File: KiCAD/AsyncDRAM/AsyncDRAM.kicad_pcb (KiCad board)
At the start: 2 copper layers, 54.6 x 33.7 mm, 14 parts, among them J1 UART, J2 SPI, J3 UPDI, J4 POWER

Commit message: Finished Routing PCB
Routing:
- net ~W: track 31.8 -> 71.0 mm, vias 2 -> 4
- net ~RAS: track 19.3 -> 47.8 mm, vias 2 -> 3
- net UPDI: track 0.00 -> 23.2 mm, vias 0 -> 1
- net ~CAS: track 28.4 -> 47.1 mm
- net +5V: track 124.1 -> 141.6 mm
- net ~OE: track 27.8 -> 43.7 mm
- net D3: track 36.5 -> 35.1 mm

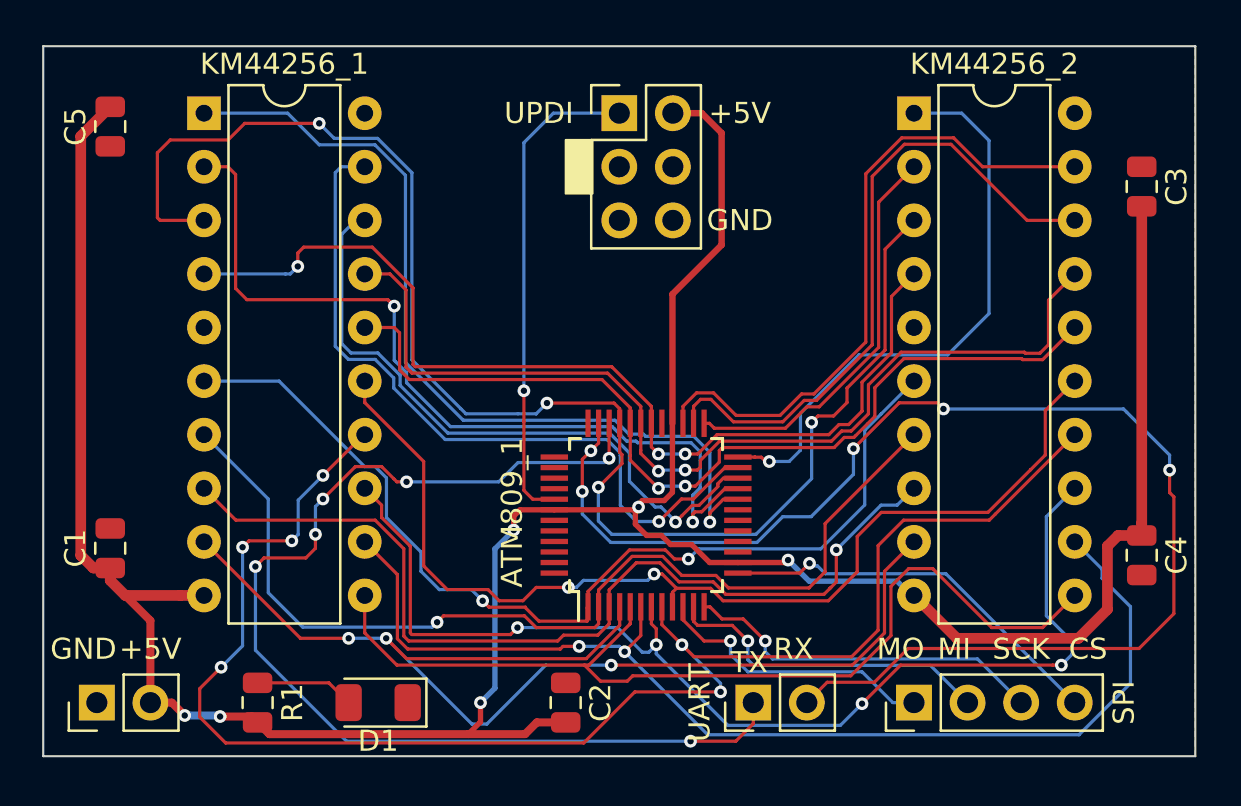
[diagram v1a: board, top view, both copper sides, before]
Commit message: Beautify the Traces + Gerber Output
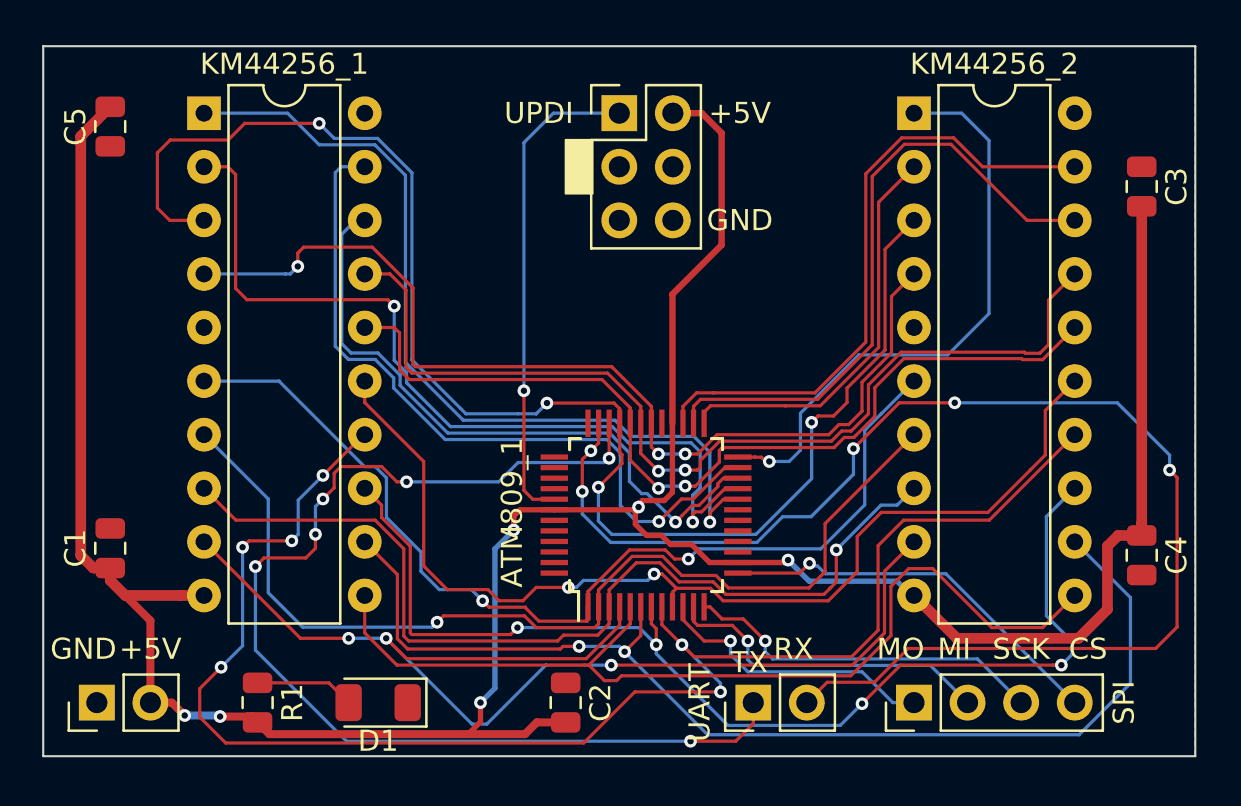
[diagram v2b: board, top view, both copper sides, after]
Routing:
- net D7: track 30.8 -> 29.9 mm
- net D6: track 31.1 -> 30.2 mm
- net RxD: track 64.4 -> 65.0 mm

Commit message: Finalized silkscreen
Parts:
- renumbered ATM809_1 to ATmega809, KM44256_1 to KM44C256BP-8, KM44256_2 to KM44C256BP-8
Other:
- board text added: "100nF"
- board text added: "470Ω"
- board text added: "47uF"
- board text added: "JLCJLCJLCJLC"

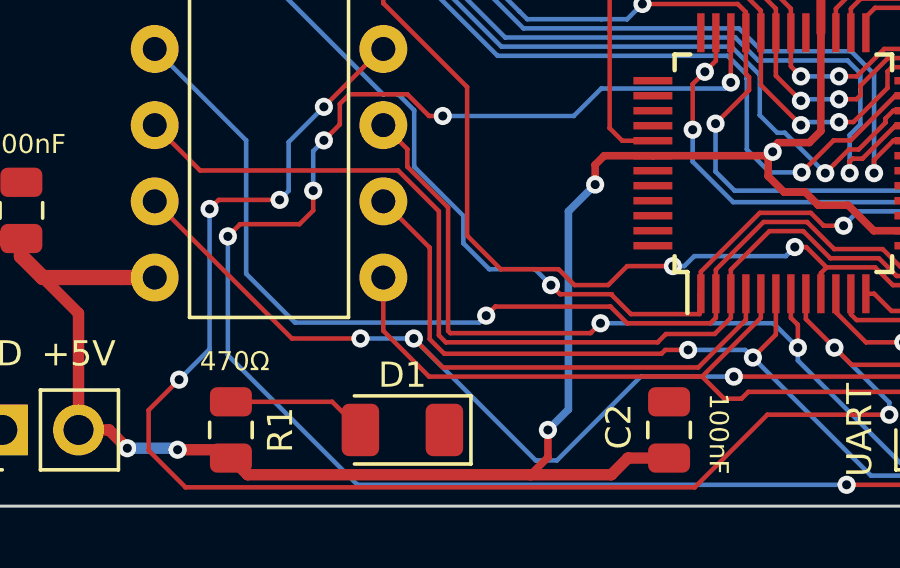
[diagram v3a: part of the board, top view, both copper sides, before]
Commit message: Re-routed power line from decoupling capacitor
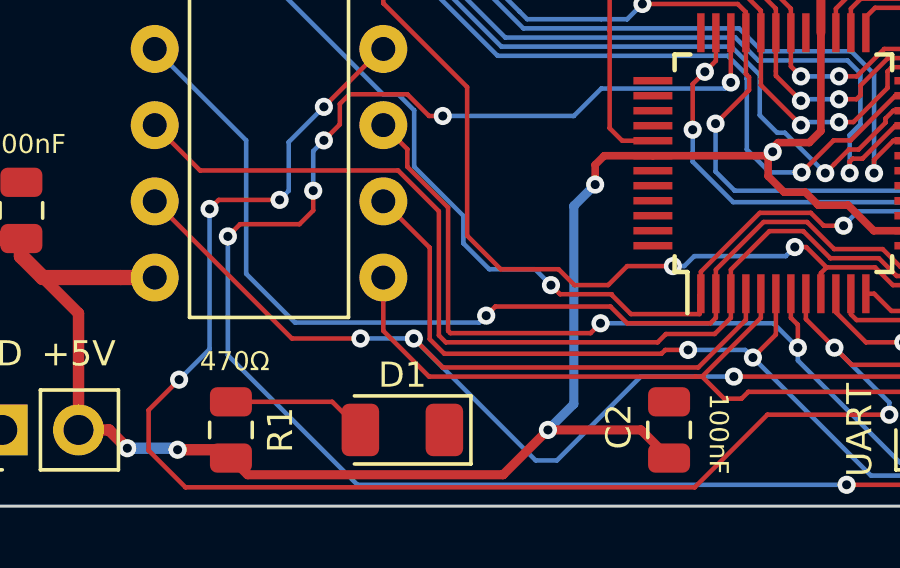
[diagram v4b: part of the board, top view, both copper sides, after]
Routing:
- net +5V: track 141.6 -> 140.6 mm
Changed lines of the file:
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@@
     (thickness 1.6)
     (drawings 23)
-    (tracks 700)
+    (tracks 698)
     (zones 0)
     (modules 14)
@@
   )
   (setup
-    (last_trace_width 0.1524)
+    (last_trace_width 0.3048)
     (user_trace_width 0.1524)
     (user_trace_width 0.2032)
@@
   (segment (start 23.5712 193.6496) (end 23.622 193.7004) (width 0.381) (layer B.Cu) (net 4))
   (segment (start 21.9456 193.6496) (end 23.5712 193.6496) (width 0.381) (layer B.Cu) (net 4))
-  (segment (start 25.4 193.9775) (end 25.956237 194.533737) (width 0.381) (layer F.Cu) (net 4))
-  (segment (start 38.6357 193.9775) (end 40.005 193.9775) (width 0.381) (layer F.Cu) (net 4))
-  (segment (start 38.079463 194.533737) (end 38.6357 193.9775) (width 0.381) (layer F.Cu) (net 4))
-  (segment (start 36.649801 185.752599) (end 36.649801 192.356599) (width 0.254) (layer B.Cu) (net 4))
-  (segment (start 37.5412 184.8612) (end 36.649801 185.752599) (width 0.254) (layer B.Cu) (net 4))
-  (segment (start 36.649801 192.356599) (end 35.9664 193.04) (width 0.254) (layer B.Cu) (net 4))
   (segment (start 35.9664 193.04) (end 35.9664 193.04) (width 0.254) (layer B.Cu) (net 4))
   (via (at 35.9664 193.04) (size 0.6048) (drill 0.3) (layers F.Cu B.Cu) (net 4))
-  (segment (start 35.9664 193.9544) (end 35.387063 194.533737) (width 0.254) (layer F.Cu) (net 4))
-  (segment (start 35.9664 193.04) (end 35.9664 193.9544) (width 0.254) (layer F.Cu) (net 4))
-  (segment (start 25.956237 194.533737) (end 35.387063 194.533737) (width 0.381) (layer F.Cu) (net 4))
-  (segment (start 35.387063 194.533737) (end 38.079463 194.533737) (width 0.381) (layer F.Cu) (net 4))
   (segment (start 58.547 189.992) (end 64.3128 189.992) (width 0.508) (layer F.Cu) (net 4))
   (segment (start 66.1901 185.1175) (end 67.31 185.1175) (width 0.508) (layer F.Cu) (net 4))
@@
   (segment (start 46.4566 165.1) (end 45.085 165.1) (width 0.3048) (layer F.Cu) (net 4))
   (segment (start 47.3964 166.0398) (end 46.4566 165.1) (width 0.3048) (layer F.Cu) (net 4))
+  (segment (start 39.0675 193.04) (end 35.9664 193.04) (width 0.3048) (layer F.Cu) (net 4))
+  (segment (start 40.005 193.9775) (end 39.0675 193.04) (width 0.3048) (layer F.Cu) (net 4))
+  (segment (start 25.956237 194.533737) (end 25.4 193.9775) (width 0.3048) (layer F.Cu) (net 4))
+  (segment (start 34.472663 194.533737) (end 25.956237 194.533737) (width 0.3048) (layer F.Cu) (net 4))
+  (segment (start 35.9664 193.04) (end 34.472663 194.533737) (width 0.3048) (layer F.Cu) (net 4))
+  (segment (start 36.83 185.5724) (end 37.5412 184.8612) (width 0.3048) (layer B.Cu) (net 4))
+  (segment (start 35.9664 193.04) (end 36.83 192.1764) (width 0.3048) (layer B.Cu) (net 4))
+  (segment (start 36.83 192.1764) (end 36.83 185.5724) (width 0.3048) (layer B.Cu) (net 4))
   (via (at 44.4246 184.4548) (size 0.6048) (drill 0.3) (layers F.Cu B.Cu) (net 8))
   (segment (start 47.547452 181.9) (end 46.059452 183.388) (width 0.1524) (layer F.Cu) (net 8))

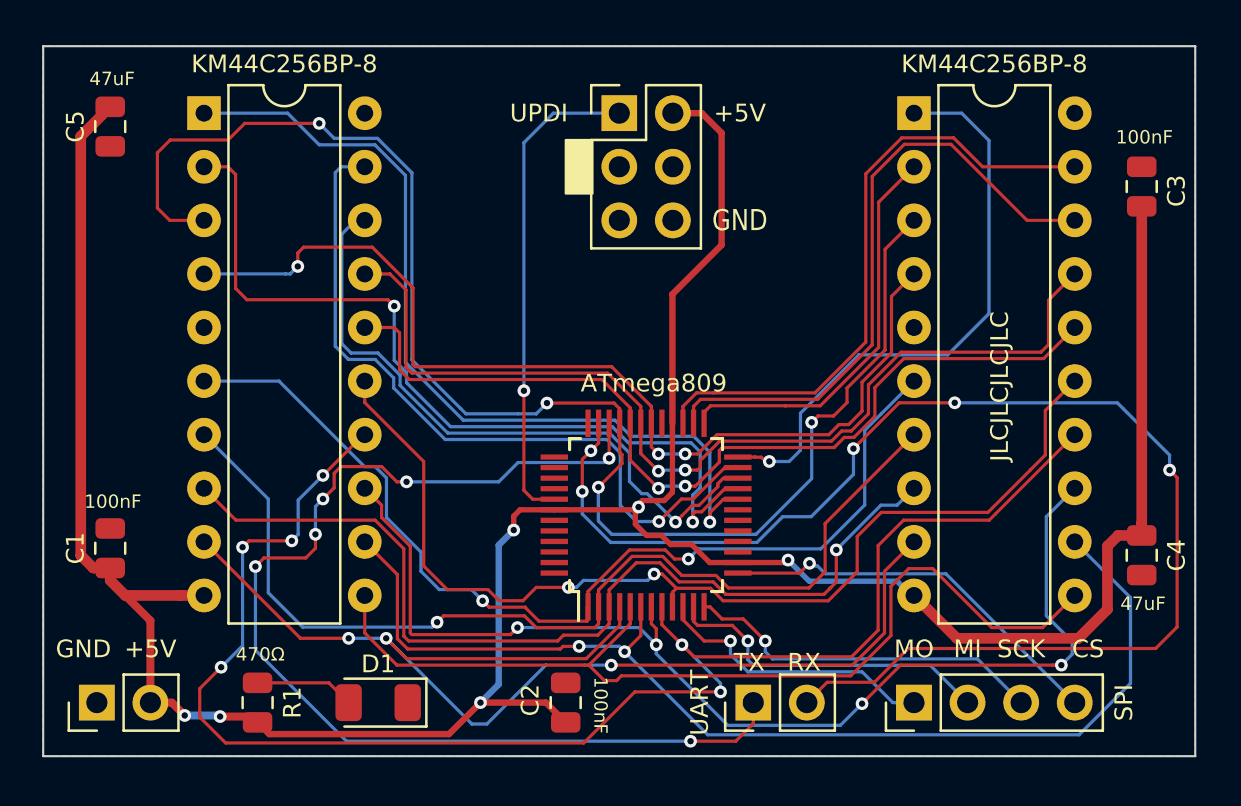
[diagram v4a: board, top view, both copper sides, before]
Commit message: Added more silk screen
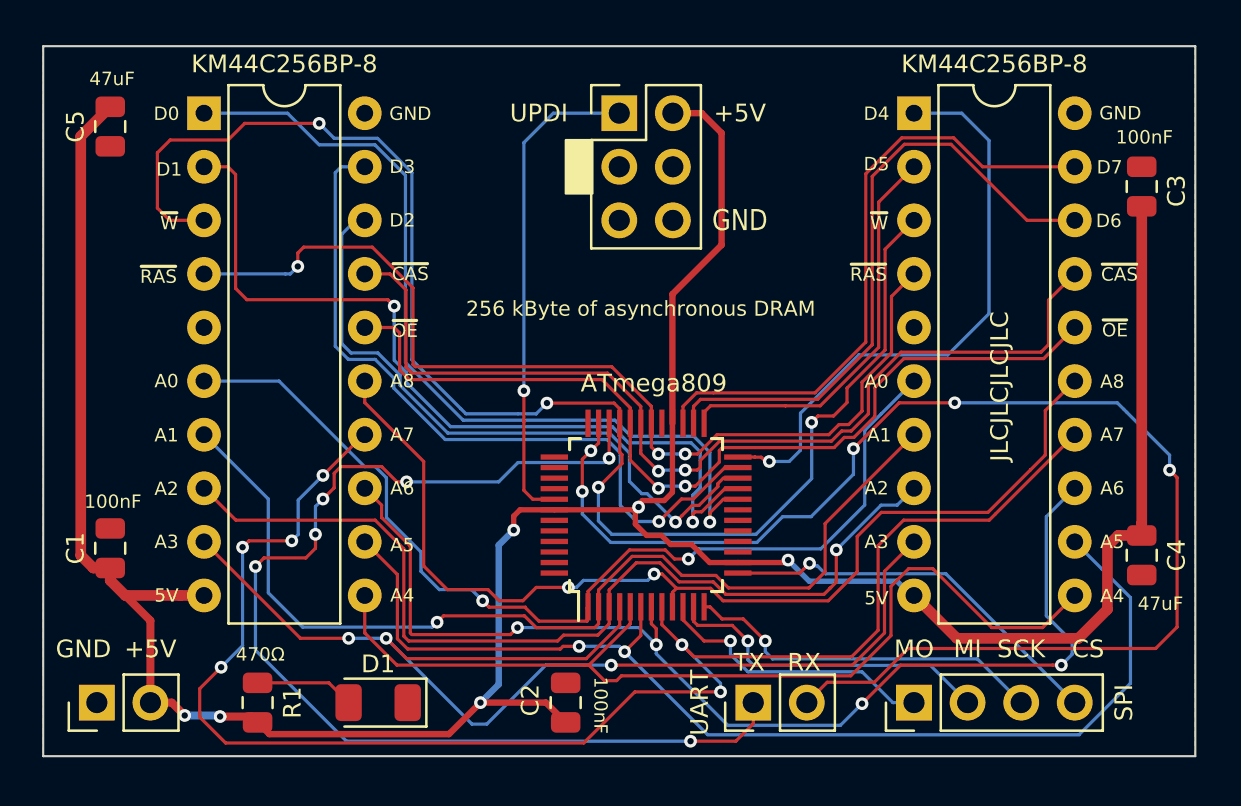
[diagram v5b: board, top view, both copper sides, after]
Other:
- board text added: "256 kByte of asynchronous DRAM"
- board text added: "5V"
- board text added: "A0"
- board text added: "A1"
- board text added: "A2"
- board text added: "A3"
- board text added: "A4"
- board text added: "A5"
- board text added: "A6"
- board text added: "A7"
- board text added: "A8"
- board text added: "D0"
- board text added: "D1"
- board text added: "D2"
- board text added: "D3"
- board text added: "D4"
- board text added: "D5"
- board text added: "D6"
- board text added: "D7"
- board text added: "~CAS"
- board text added: "~OE"
- board text added: "~RAS"
- board text added: "~W"
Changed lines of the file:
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@@
   (general
     (thickness 1.6)
-    (drawings 23)
+    (drawings 62)
     (tracks 698)
     (zones 0)
@@
   )
   (setup
-    (last_trace_width 0.3048)
+    (last_trace_width 0.1524)
     (user_trace_width 0.1524)
     (user_trace_width 0.2032)
@@
     )
   )
+  (gr_text "256 kByte of asynchronous DRAM" (at 43.561 174.371) (layer F.SilkS)
+    (effects (font (size 0.7112 0.7112) (thickness 0.15)))
+  )
+  (gr_text A4 (at 65.913 187.9854) (layer F.SilkS)
+    (effects (font (size 0.635 0.635) (thickness 0.15)))
+  )
+  (gr_text A5 (at 65.913 185.42) (layer F.SilkS)
+    (effects (font (size 0.635 0.635) (thickness 0.15)))
+  )
+  (gr_text A6 (at 65.913 182.88) (layer F.SilkS)
+    (effects (font (size 0.635 0.635) (thickness 0.15)))
+  )
+  (gr_text A7 (at 65.913 180.34) (layer F.SilkS)
+    (effects (font (size 0.635 0.635) (thickness 0.15)))
+  )
+  (gr_text A8 (at 65.913 177.8254) (layer F.SilkS)
+    (effects (font (size 0.635 0.635) (thickness 0.15)))
+  )
+  (gr_text ~OE (at 66.04 175.387) (layer F.SilkS)
+    (effects (font (size 0.635 0.635) (thickness 0.15)))
+  )
+  (gr_text ~CAS (at 66.2559 172.7454) (layer F.SilkS)
+    (effects (font (size 0.635 0.635) (thickness 0.15)))
+  )
+  (gr_text D6 (at 65.7479 170.2054) (layer F.SilkS)
+    (effects (font (size 0.635 0.635) (thickness 0.15)))
+  )
+  (gr_text D7 (at 65.786 167.6654) (layer F.SilkS)
+    (effects (font (size 0.635 0.635) (thickness 0.15)))
+  )
+  (gr_text GND (at 66.294 165.1) (layer F.SilkS)
+    (effects (font (size 0.635 0.635) (thickness 0.15)))
+  )
+  (gr_text 5V (at 54.737 188.087) (layer F.SilkS)
+    (effects (font (size 0.635 0.635) (thickness 0.15)))
+  )
+  (gr_text A3 (at 54.737 185.42) (layer F.SilkS)
+    (effects (font (size 0.635 0.635) (thickness 0.15)))
+  )
+  (gr_text A2 (at 54.737 182.88) (layer F.SilkS)
+    (effects (font (size 0.635 0.635) (thickness 0.15)))
+  )
+  (gr_text A1 (at 54.864 180.3654) (layer F.SilkS)
+    (effects (font (size 0.635 0.635) (thickness 0.15)))
+  )
+  (gr_text A0 (at 54.737 177.8254) (layer F.SilkS)
+    (effects (font (size 0.635 0.635) (thickness 0.15)))
+  )
+  (gr_text ~RAS (at 54.356 172.7454) (layer F.SilkS)
+    (effects (font (size 0.635 0.635) (thickness 0.15)))
+  )
+  (gr_text ~W (at 54.864 170.307) (layer F.SilkS)
+    (effects (font (size 0.635 0.635) (thickness 0.15)))
+  )
+  (gr_text D5 (at 54.737 167.513) (layer F.SilkS)
+    (effects (font (size 0.635 0.635) (thickness 0.15)))
+  )
+  (gr_text D4 (at 54.737 165.1254) (layer F.SilkS)
+    (effects (font (size 0.635 0.635) (thickness 0.15)))
+  )
+  (gr_text A4 (at 32.258 187.96) (layer F.SilkS)
+    (effects (font (size 0.635 0.635) (thickness 0.15)))
+  )
+  (gr_text A5 (at 32.258 185.5724) (layer F.SilkS)
+    (effects (font (size 0.635 0.635) (thickness 0.15)))
+  )
+  (gr_text A6 (at 32.258 182.88) (layer F.SilkS)
+    (effects (font (size 0.635 0.635) (thickness 0.15)))
+  )
+  (gr_text A7 (at 32.258 180.34) (layer F.SilkS)
+    (effects (font (size 0.635 0.635) (thickness 0.15)))
+  )
+  (gr_text A8 (at 32.258 177.8) (layer F.SilkS)
+    (effects (font (size 0.635 0.635) (thickness 0.15)))
+  )
+  (gr_text ~OE (at 32.385 175.4124) (layer F.SilkS)
+    (effects (font (size 0.635 0.635) (thickness 0.15)))
+  )
+  (gr_text ~CAS (at 32.639 172.72) (layer F.SilkS)
+    (effects (font (size 0.635 0.635) (thickness 0.15)))
+  )
+  (gr_text D2 (at 32.258 170.18) (layer F.SilkS)
+    (effects (font (size 0.635 0.635) (thickness 0.15)))
+  )
+  (gr_text D3 (at 32.258 167.64) (layer F.SilkS)
+    (effects (font (size 0.635 0.635) (thickness 0.15)))
+  )
+  (gr_text GND (at 32.639 165.1254) (layer F.SilkS)
+    (effects (font (size 0.635 0.635) (thickness 0.15)))
+  )
+  (gr_text 5V (at 21.082 187.96) (layer F.SilkS)
+    (effects (font (size 0.635 0.635) (thickness 0.15)))
+  )
+  (gr_text A3 (at 21.082 185.42) (layer F.SilkS)
+    (effects (font (size 0.635 0.635) (thickness 0.15)))
+  )
+  (gr_text A2 (at 21.082 182.9054) (layer F.SilkS)
+    (effects (font (size 0.635 0.635) (thickness 0.15)))
+  )
+  (gr_text A1 (at 21.082 180.3654) (layer F.SilkS)
+    (effects (font (size 0.635 0.635) (thickness 0.15)))
+  )
+  (gr_text A0 (at 21.082 177.8) (layer F.SilkS)
+    (effects (font (size 0.635 0.635) (thickness 0.15)))
+  )
+  (gr_text ~RAS (at 20.701 172.847) (layer F.SilkS)
+    (effects (font (size 0.635 0.635) (thickness 0.15)))
+  )
+  (gr_text ~W (at 21.209 170.307) (layer F.SilkS)
+    (effects (font (size 0.635 0.635) (thickness 0.15)))
+  )
+  (gr_text D1 (at 21.209 167.767) (layer F.SilkS)
+    (effects (font (size 0.635 0.635) (thickness 0.15)))
+  )
+  (gr_text D0 (at 21.082 165.1254) (layer F.SilkS)
+    (effects (font (size 0.635 0.635) (thickness 0.15)))
+  )
   (gr_text JLCJLCJLCJLC (at 60.579 178.054 90) (layer F.SilkS)
     (effects (font (size 0.8382 0.8382) (thickness 0.15)))
@@
     (effects (font (size 0.635 0.635) (thickness 0.15)))
   )
-  (gr_text 47uF (at 67.3735 188.3537) (layer F.SilkS)
-    (effects (font (size 0.635 0.635) (thickness 0.15)))
-  )
+  (gr_text 47uF (at 68.199 188.3537) (layer F.SilkS)
+    (effects (font (size 0.635 0.635) (thickness 0.15)))
+  )
